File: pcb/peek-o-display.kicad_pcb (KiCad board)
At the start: 2 copper layers, 102.9 x 53.3 mm, 8 parts, among them J1 Conn_02x15_Odd_Even

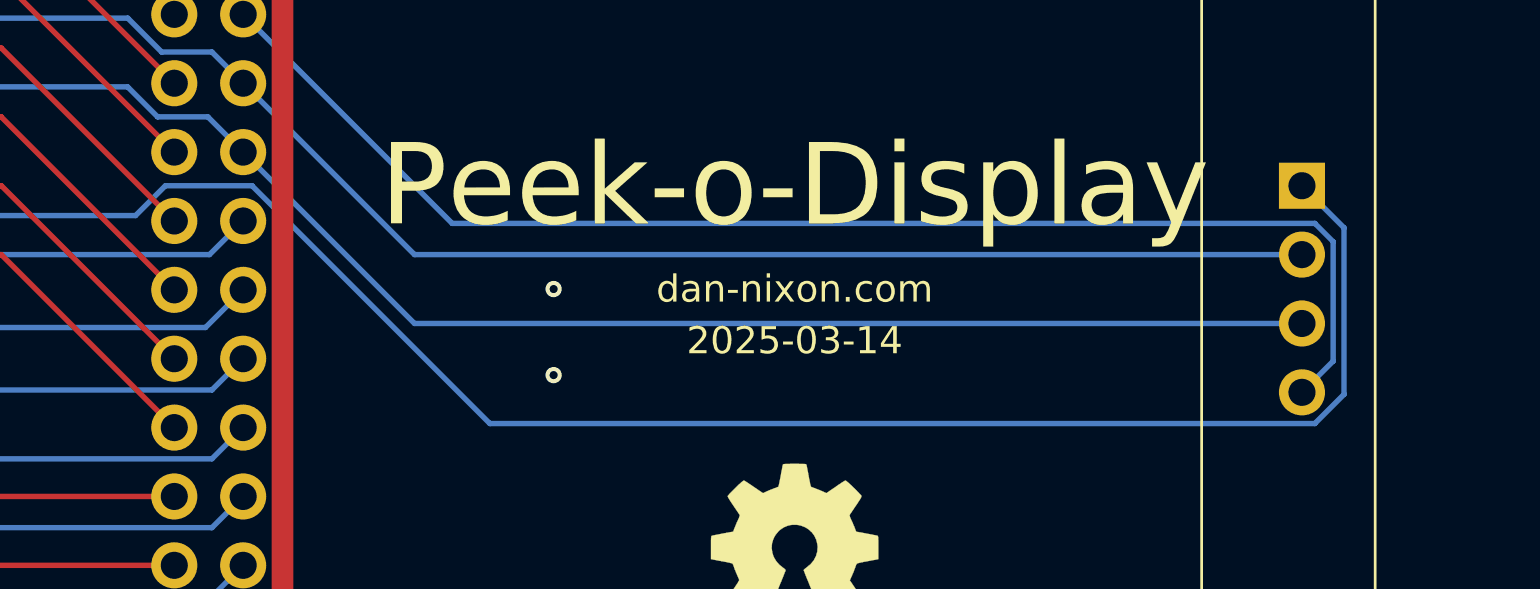
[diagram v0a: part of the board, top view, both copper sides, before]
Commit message: Slot SD card SPI holes on display module
Addresses the fact that not all modules seem to have the same distance
between the two banks of pin headers.
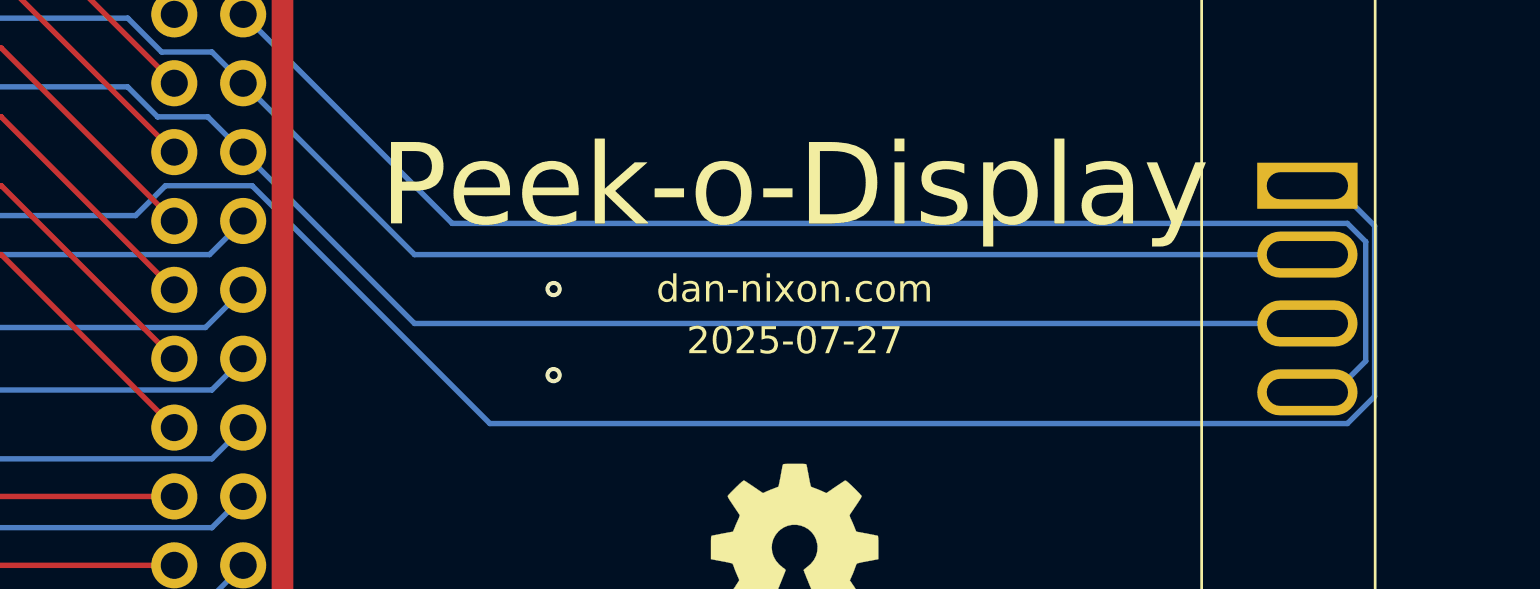
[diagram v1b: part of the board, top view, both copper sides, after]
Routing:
- net /SPI_CLK: track 117.5 -> 119.7 mm
- net /SD_CS: track 90.7 -> 92.9 mm
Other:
- board text added: "2025-07-27"
- board text removed: "2025-03-14"
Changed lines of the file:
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@@
 		)
 		(pad "15" thru_hole rect
-			(at -3.81 -40.3)
-			(size 1.7 1.7)
-			(drill 1)
+			(at -3.81 -40.5)
+			(size 3.7 1.7)
+			(drill oval 3 1)
 			(layers "*.Cu" "*.Mask")
 			(remove_unused_layers no)
@@
 		)
 		(pad "16" thru_hole oval
-			(at -1.27 -40.3)
-			(size 1.7 1.7)
-			(drill 1)
+			(at -1.27 -40.5)
+			(size 3.7 1.7)
+			(drill oval 3 1)
 			(layers "*.Cu" "*.Mask")
 			(remove_unused_layers no)
@@
 		)
 		(pad "17" thru_hole oval
-			(at 1.27 -40.3)
-			(size 1.7 1.7)
-			(drill 1)
+			(at 1.27 -40.5)
+			(size 3.7 1.7)
+			(drill oval 3 1)
 			(layers "*.Cu" "*.Mask")
 			(remove_unused_layers no)
@@
 		)
 		(pad "18" thru_hole oval
-			(at 3.81 -40.3)
-			(size 1.7 1.7)
-			(drill 1)
+			(at 3.81 -40.5)
+			(size 3.7 1.7)
+			(drill oval 3 1)
 			(layers "*.Cu" "*.Mask")
 			(remove_unused_layers no)
@@
 		)
 	)
-	(gr_text "2025-03-14"
+	(gr_text "2025-07-27"
 		(at 148.59 102.235 0)
 		(layer "F.SilkS")
@@
 	)
 	(segment
-		(start 128.57776 96.52)
+		(start 168.97676 105.291)
+		(end 169.979 104.28876)
+		(width 0.2)
+		(layer "B.Cu")
+		(net 11)
+	)
+	(segment
+		(start 91.44 96.52)
+		(end 92.541 97.621)
+		(width 0.2)
+		(layer "B.Cu")
+		(net 11)
+	)
+	(segment
+		(start 124.28124 97.621)
 		(end 125.38224 96.52)
 		(width 0.2)
@@
 	)
 	(segment
-		(start 168.852 98.072)
-		(end 168.852 104.21576)
+		(start 168.5 96.52)
+		(end 167.5 96.52)
 		(width 0.2)
 		(layer "B.Cu")
@@
 	)
 	(segment
-		(start 167.77676 105.291)
-		(end 137.34876 105.291)
+		(start 169.979 97.999)
+		(end 168.5 96.52)
 		(width 0.2)
 		(layer "B.Cu")
@@
 	)
 	(segment
-		(start 168.852 104.21576)
-		(end 167.77676 105.291)
+		(start 169.979 104.28876)
+		(end 169.979 97.999)
+		(width 0.2)
+		(layer "B.Cu")
+		(net 11)
+	)
+	(segment
+		(start 125.38224 96.52)
+		(end 128.57776 96.52)
+		(width 0.2)
+		(layer "B.Cu")
+		(net 11)
+	)
+	(segment
+		(start 137.34876 105.291)
+		(end 168.97676 105.291)
 		(width 0.2)
 		(layer "B.Cu")
@@
 	)
 	(segment
-		(start 91.44 96.52)
-		(end 92.541 97.621)
-		(width 0.2)
-		(layer "B.Cu")
-		(net 11)
-	)
-	(segment
-		(start 124.28124 97.621)
-		(end 125.38224 96.52)
-		(width 0.2)
-		(layer "B.Cu")
-		(net 11)
-	)
-	(segment
-		(start 167.3 96.52)
-		(end 168.852 98.072)
-		(width 0.2)
-		(layer "B.Cu")
-		(net 11)
-	)
-	(segment
-		(start 137.34876 105.291)
-		(end 128.57776 96.52)
+		(start 128.57776 96.52)
+		(end 137.34876 105.291)
 		(width 0.2)
 		(layer "B.Cu")
@@
 	)
 	(segment
-		(start 168.451 98.58324)
-		(end 168.451 102.989)
+		(start 169.651 98.58324)
+		(end 169.651 102.989)
+		(width 0.2)
+		(layer "B.Cu")
+		(net 23)
+	)
+	(segment
+		(start 169.651 102.989)
+		(end 168.5 104.14)
 		(width 0.2)
 		(layer "B.Cu")
@@
 	)
 	(segment
+		(start 168.97676 97.909)
+		(end 169.651 98.58324)
+		(width 0.2)
+		(layer "B.Cu")
+		(net 23)
+	)
+	(segment
+		(start 135.959 97.909)
+		(end 168.97676 97.909)
+		(width 0.2)
+		(layer "B.Cu")
+		(net 23)
+	)
+	(segment
 		(start 123.994 87.799)
 		(end 125.244 89.049)
@@
 	)
 	(segment
-		(start 167.77676 97.909)
-		(end 168.451 98.58324)
-		(width 0.2)
-		(layer "B.Cu")
-		(net 23)
-	)
-	(segment
-		(start 168.451 102.989)
-		(end 167.3 104.14)
+		(start 91.44 83.82)
+		(end 95.419 87.799)
 		(width 0.2)
 		(layer "B.Cu")
@@
 	)
 	(segment
-		(start 91.44 83.82)
-		(end 95.419 87.799)
-		(width 0.2)
-		(layer "B.Cu")
-		(net 23)
-	)
-	(segment
-		(start 135.959 97.909)
-		(end 167.77676 97.909)
-		(width 0.2)
-		(layer "B.Cu")
+		(start 168.5 104.14)
+		(end 167.5 104.14)
+		(width 0.2)
+		(layer "B.Cu")
